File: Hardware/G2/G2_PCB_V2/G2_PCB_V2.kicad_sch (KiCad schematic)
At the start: 36 parts, among them J1 Programador, J2 TB_1X2, J6 Sharp_Der, J6 Sharp_Frontal, J6 Sharp_Izq, U1 ESP32-WROOM-32, U1 MPU-9150, U3 AMS1117-3.3, U3 AMS1117-5, U5 DRV8833

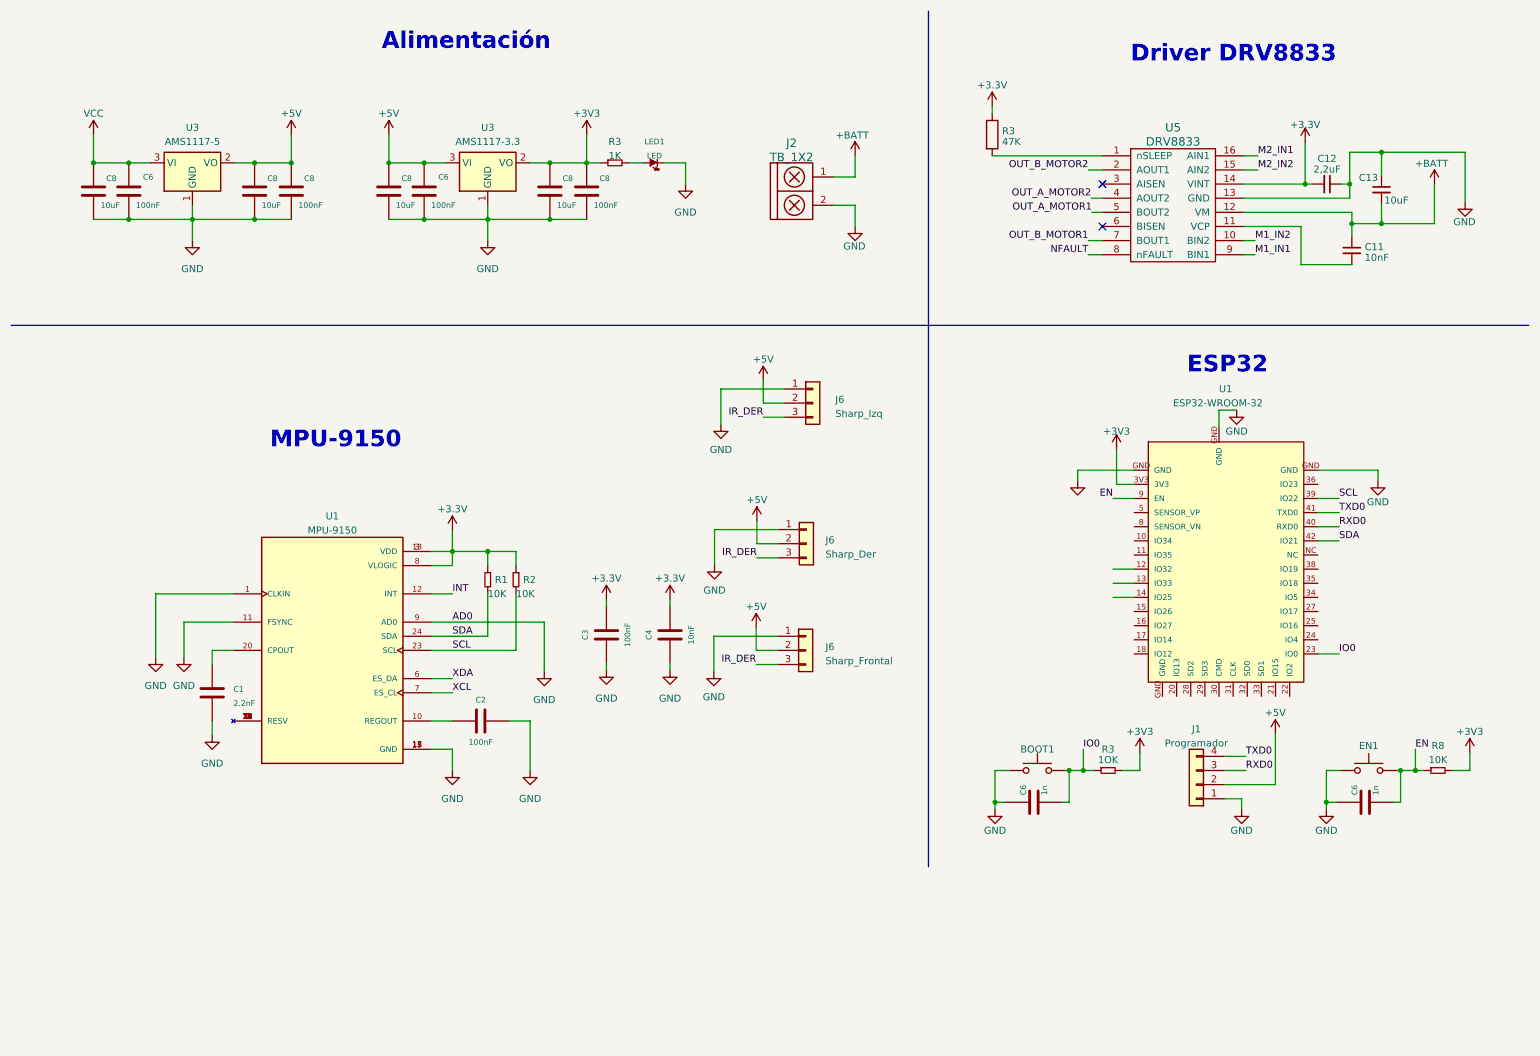
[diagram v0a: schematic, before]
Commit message: agregue la version final de la mpu9150 y la version final del Pla version 2 del PCB
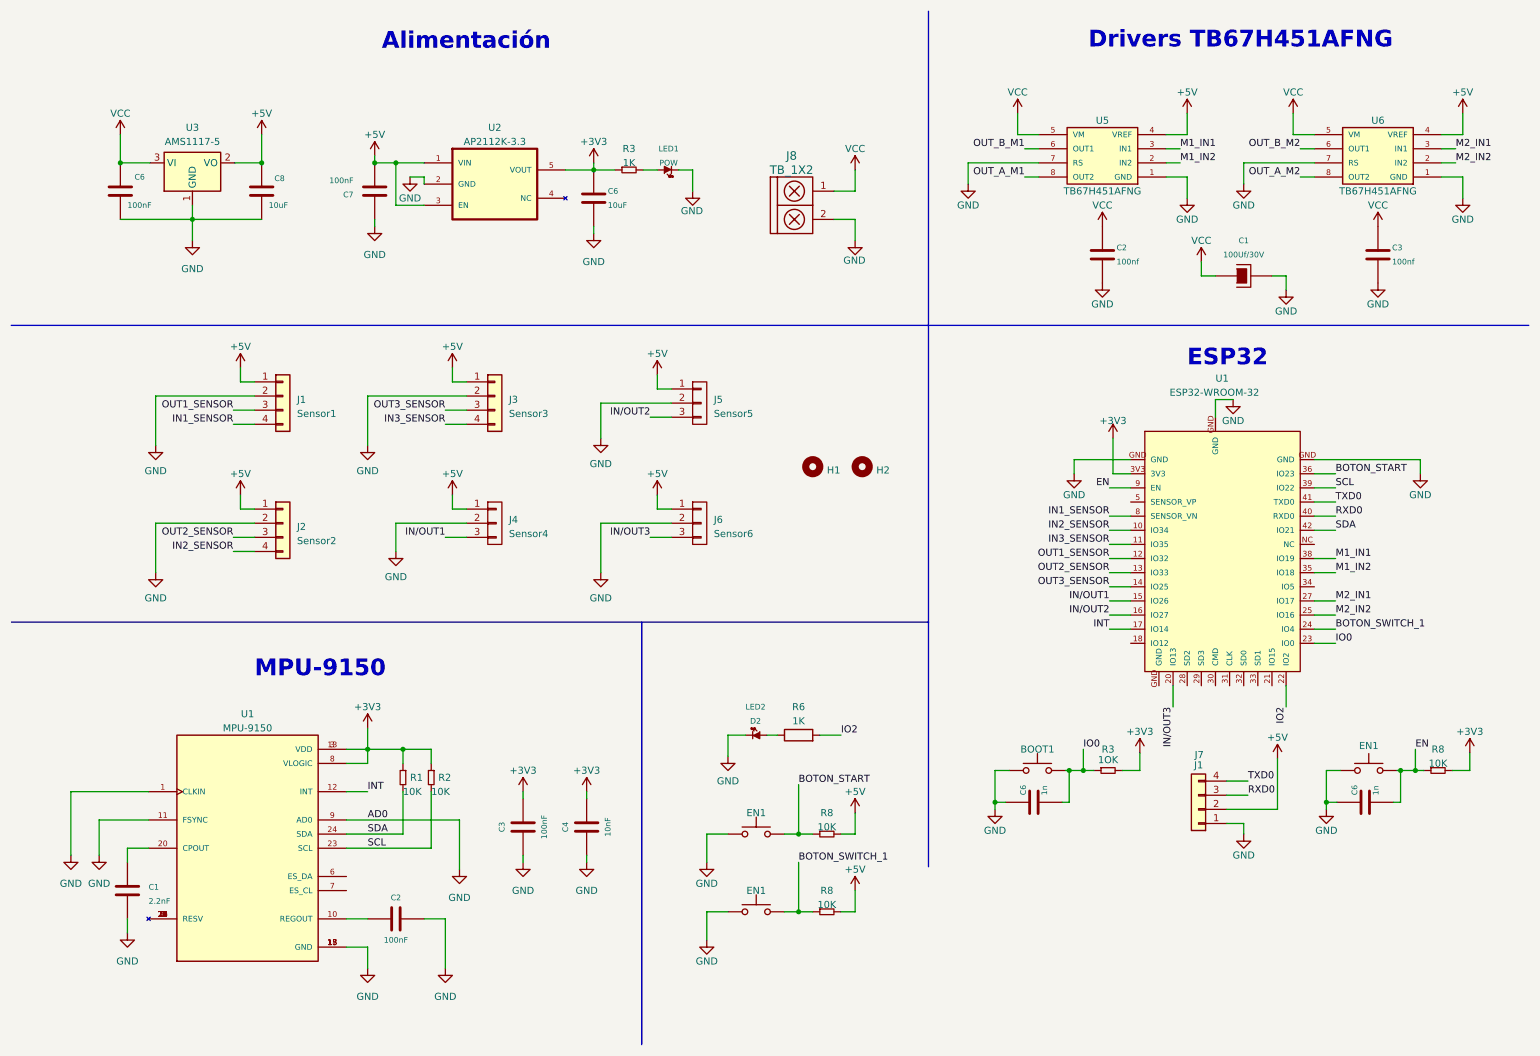
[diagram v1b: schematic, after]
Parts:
- removed C11: 10nF, EESTN5:C_1206, symbol Device:C_Small
- removed C12: 2,2uF, EESTN5:C_1206, symbol Device:C_Small
- removed C13: 10uF, EESTN5:C_1206, symbol Device:C_Small
- removed C8 (x3): 10uF, EESTN5:C_0805, symbol EESTN5:C
- removed C8 (x2): 100nF, EESTN5:C_0805, symbol EESTN5:C
- removed J6: Sharp_Der, Connector_JST:JST_EH_B3B-EH-A_1x03_P2.50mm_Vertical, symbol Connector_Generic:Conn_01x03
- removed J6: Sharp_Izq, Connector_JST:JST_EH_B3B-EH-A_1x03_P2.50mm_Vertical, symbol Connector_Generic:Conn_01x03
- removed J6: Sharp_Frontal, Connector_JST:JST_EH_B3B-EH-A_1x03_P2.50mm_Vertical, symbol Connector_Generic:Conn_01x03
- removed R3: 47K, EESTN5:R_1206, symbol Device:R
- removed U3: AMS1117-3.3, footprints:SOT-223-3_TabPin2, symbol Regulator_Linear:AMS1117-3.3
- removed U5: DRV8833, symbol EESTN5:DRV8833
- added C1: 100Uf/30V, EESTN5:CAP_ELEC_5x11mm, symbol EESTN5:CAPAPOL
- added C2, C3: 100nf, EESTN5:C_0805, symbol EESTN5:C
- added C7: 100nF, footprints:C_0603, symbol EESTN5:C
- added EN1 (x2): SW_Push, EESTN5:Pulsador_SMD_2_ALTO, symbol EESTN5:SW_Push
- added H1, H2: Mounting_Hole, EESTN5:pad_3mm, symbol EESTN5:Mounting_Hole
- added J1: Sensor1, EESTN5:pin_strip_4, symbol EESTN5:Conn_01x04
- added J2: Sensor2, EESTN5:pin_strip_4, symbol EESTN5:Conn_01x04
- added J3: Sensor3, EESTN5:pin_strip_4, symbol EESTN5:Conn_01x04
- added J4: Sensor4, EESTN5:Pin_Header_3, symbol EESTN5:Conn_01X03
- added J5: Sensor5, EESTN5:Pin_Header_3, symbol EESTN5:Conn_01X03
- added J6: Sensor6, EESTN5:Pin_Header_3, symbol EESTN5:Conn_01X03
- added LED2: D2, EESTN5:Led_0805, symbol EESTN5:LED
- added R6: 1K, footprints:R_0603, symbol Device:R
- added R8 (x2): 10K, footprints:R_0603, symbol EESTN5:R
- added U2: AP2112K-3.3, footprints:AP2112K-3.3-Sot25, symbol Librerias:AP2112K-3.3
- added U5, U6: TB67H451AFNG, footprints:TB67H451AFNG, symbol Librerias:TB67H451AFNG
- BOOT1, EN1: footprint footprints:Button -> EESTN5:Pulsador_SMD_2_ALTO
- C6: footprint EESTN5:C_0805 -> footprints:C_0603
- C6: value 100nF -> 10uF; footprint EESTN5:C_0805 -> footprints:C_0603
- J1: value Programador -> J7
- J8: renamed from J2; footprint (none) -> EESTN5:BORNERA2_AZUL
- LED1: value LED -> POW
- R1, R2, R3: footprint EESTN5:R_0805 -> footprints:R_0603
- R3, R8: footprint EESTN5:R_1206 -> footprints:R_0603
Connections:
- net +3.3V is gone; now on net +3V3: C3.1, C4.1, R1.1, R2.1, U1.13 (VDD), U1.3 (VDD), U1.8 (VLOGIC)
- net +BATT is gone; now on net VCC: J8.1
- net +3V3: now also C6.2, U2.5 (VOUT)
- net +5V: now also C7.1, J1.1 (Pin_1), J2.1 (Pin_1), J3.1 (Pin_1), J4.1 (P1), J5.1 (P1), J6.1 (P1), R8.2, R8.2, U2.1 (VIN), U2.3 (EN), U5.4 (VREF), U6.4 (VREF); no longer C6.1
- net GND: now also C6.1, C1.2, C2.2, C3.2, C7.2, EN1.1, EN1.1, J1.2 (Pin_2), J2.2 (Pin_2), J3.2 (Pin_2), J4.2 (P2), J5.2 (P2), J6.2 (P2), LED2.2 (K), U2.2 (GND), U5.1 (GND), U5.7 (RS), U6.1 (GND), U6.7 (RS); no longer C6.2
- net INT: now also U1.17 (IO14)
- net M1_IN1: now also U1.38 (IO19), U5.3 (IN1)
- net M1_IN2: now also U1.35 (IO18), U5.2 (IN2)
- net M2_IN1: now also U1.27 (IO17), U6.3 (IN1)
- net M2_IN2: now also U1.25 (IO16), U6.2 (IN2)
- net VCC: now also C1.1, C2.1, C3.1, U5.5 (VM), U6.5 (VM)
- net IN2_SENSOR: now reaches U1.10 (IO34)
- net IN2_SENSOR: now also J2.4 (Pin_4)
- net IN3_SENSOR: now reaches U1.11 (IO35)
- net IN3_SENSOR: now also J3.4 (Pin_4)
- net OUT1_SENSOR: now reaches U1.12 (IO32)
- net OUT1_SENSOR: now also J1.3 (Pin_3)
- net OUT2_SENSOR: now reaches U1.13 (IO33)
- net OUT2_SENSOR: now also J2.3 (Pin_3)
- net OUT3_SENSOR: now reaches U1.14 (IO25)
- net OUT3_SENSOR: now also J3.3 (Pin_3)
- net IN/OUT1: now reaches U1.15 (IO26)
- net IN/OUT1: now also J4.3 (P3)
- net IN/OUT2: now reaches U1.16 (IO27)
- net IN/OUT2: now also J5.3 (P3)
- net IN/OUT3: now reaches U1.20 (IO13)
- net IN/OUT3: now also J6.3 (P3)
- net IO2: now reaches U1.22 (IO2)
- net IO2: now also R6.2
- net BOTON_SWITCH_1: now reaches U1.24 (IO4)
- net BOTON_SWITCH_1: now also EN1.2, R8.1
- net BOTON_START: now reaches U1.36 (IO23)
- net BOTON_START: now also EN1.2, R8.1
- net IN1_SENSOR: now reaches U1.8 (SENSOR_VN)
- net IN1_SENSOR: now also J1.4 (Pin_4)
- net XCL: no longer names the net of U1.7 (ES_CL)
- net XDA: no longer names the net of U1.6 (ES_DA)
- new net: LED2.1 (A), R6.1
- new net OUT_A_M1: U5.8 (OUT2)
- new net OUT_A_M2: U6.8 (OUT2)
- new net OUT_B_M1: U5.6 (OUT1)
- new net OUT_B_M2: U6.6 (OUT1)
- no-connect marks 2 -> 0
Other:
- note added: "Drivers TB67H451AFNG"
- note removed: "Driver DRV8833"
- moved on the sheet: C1, C2, C3, C4, C6, C8, J1, J8, R1, R2, U1
